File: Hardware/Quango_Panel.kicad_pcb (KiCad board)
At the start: 2 copper layers, 80.9 x 128.5 mm, 25 parts

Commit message: More schematic updates
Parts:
- added Ref**: Subminiature_Switch, Custom_Footprints:LED_Hole_3mm, F.Cu at (106.1, 42.6)
- added Ref**: Subminiature_Switch, Custom_Footprints:LED_Hole_3mm, F.Cu at (77.8, 42.6)
- added Ref**: Subminiature_Switch, Custom_Footprints:LED_Hole_3mm, F.Cu at (86.2, 42.6)
- added Ref**: Subminiature_Switch, Custom_Footprints:LED_Hole_3mm, F.Cu at (97.7, 42.6)
- moved REF** 21.2 mm to (100.3, 139.2)
- moved USB** 17.6 mm to (81.5, 141.1)
- moved Ref** 10.7 mm to (81.7, 127.7)
- moved REF** 9.72 mm to (80.0, 118.4)
- moved REF** 9.72 mm to (96.2, 118.6)
- moved Ref** 8.41 mm to (73.6, 42.6), turned to 90 degrees
- moved RESET 7.21 mm to (79.8, 48.6)
- moved RESET 6.28 mm to (100.0, 48.6)
- moved Ref** 5.61 mm to (101.9, 42.6), turned to 90 degrees
- moved Ref** 4.78 mm to (82.0, 42.6), turned to 90 degrees
- moved Ref** 2.01 mm to (93.5, 42.6), turned to 90 degrees

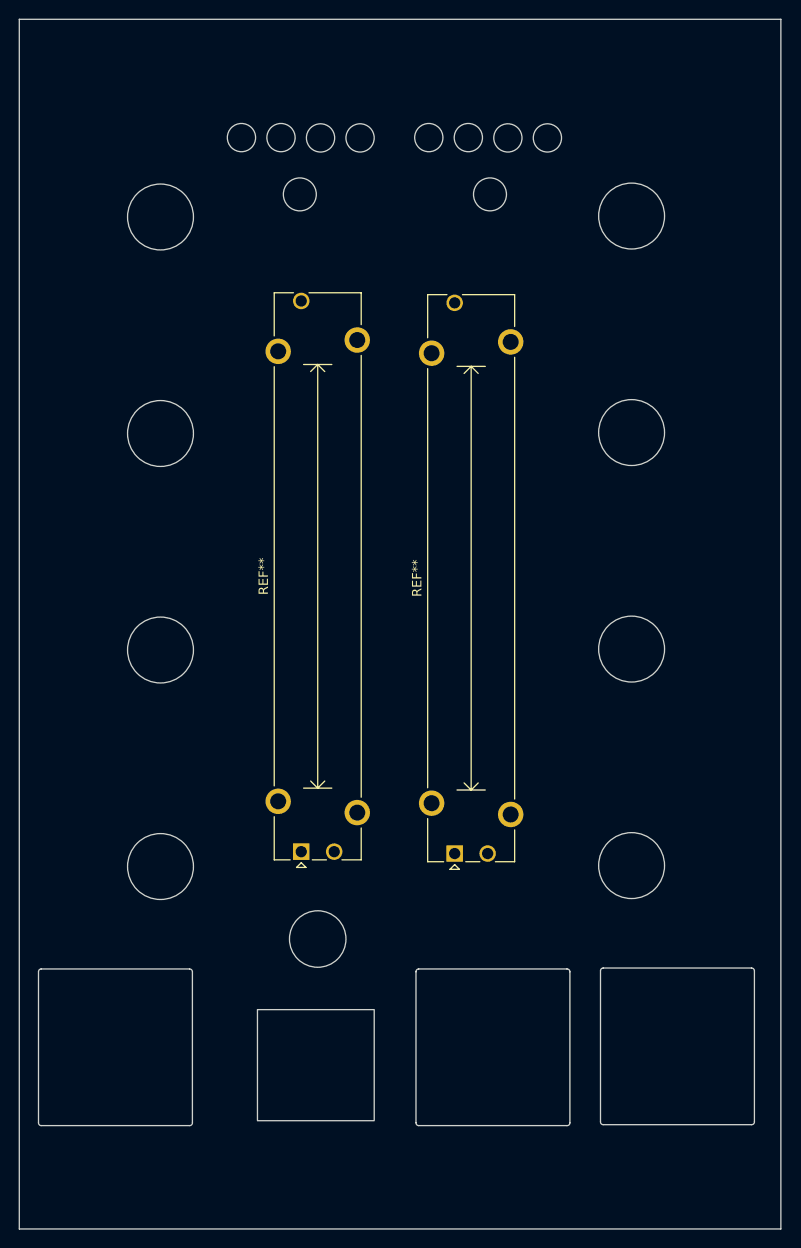
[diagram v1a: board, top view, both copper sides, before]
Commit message: Reduced module size to 14HP; updated to Amphenol USB C
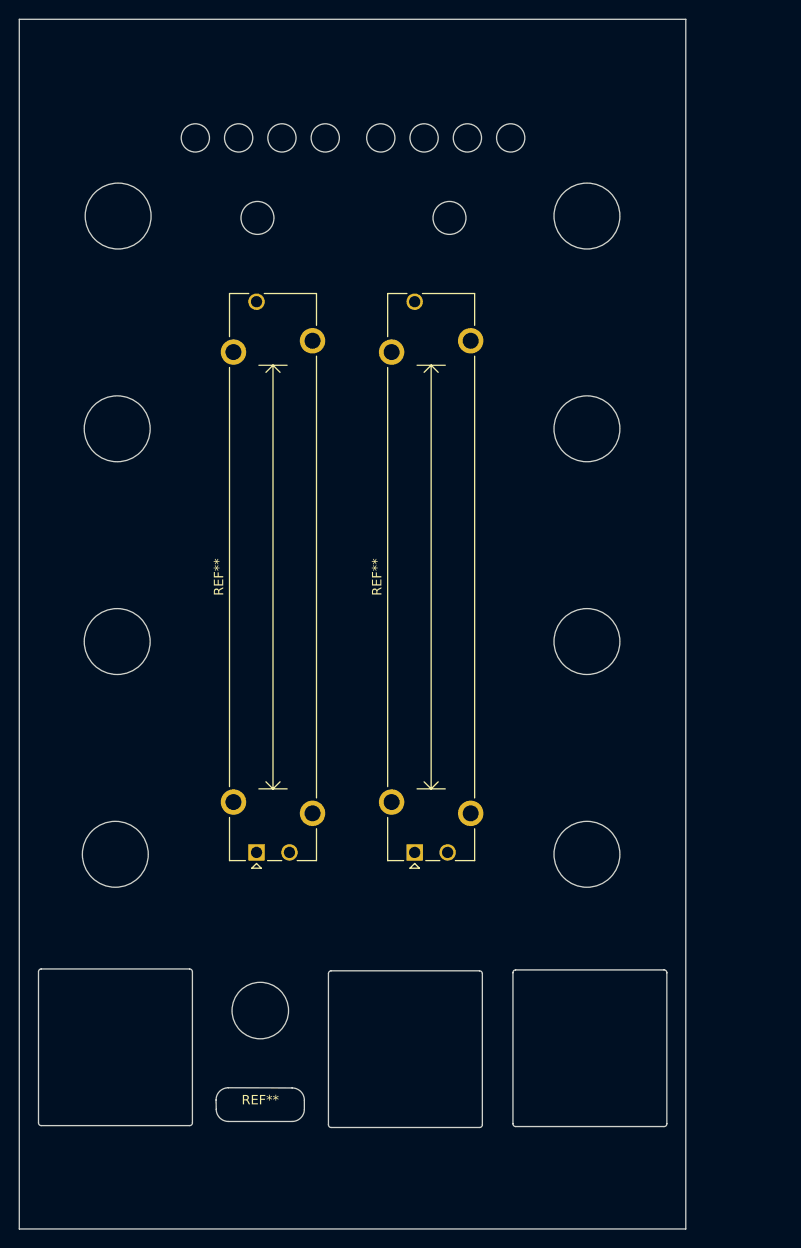
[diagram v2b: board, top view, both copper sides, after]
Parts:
- removed USB**: USB_B_CUTOUT, Custom_Footprints:USB_B_CUTOUT
- added REF**: USB_C_Cutout, Custom_Footprints:USB_C_Cutout, F.Cu at (75.6, 145.3)
- moved Ref** 9.75 mm to (75.6, 135.3)
- moved REF** 9.30 mm to (110.6, 139.3)
- moved REF** 9.30 mm to (91.0, 139.4)
- moved RESET 5.15 mm to (75.3, 51.1)
- moved Ref** 5.10 mm to (88.4, 42.6)
- moved RESET 4.97 mm to (95.7, 51.1)
- moved Ref** 4.97 mm to (60.2, 118.7)
- moved Ref** 4.90 mm to (68.7, 42.6)
- moved Ref** 4.89 mm to (110.3, 118.7)
- moved Ref** 4.81 mm to (110.3, 96.1)
- moved Ref** 4.76 mm to (110.3, 73.5)
- moved REF** 4.75 mm to (75.2, 118.5)
- moved Ref** 4.74 mm to (110.3, 50.9)
- moved Ref** 4.70 mm to (93.0, 42.6)
- moved Ref** 4.69 mm to (60.4, 96.1)
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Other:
- board size 80.9 x 128.5 mm -> 70.8 x 128.5 mm
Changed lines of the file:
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@@
   (net 0 "")
   (footprint "Custom_Footprints:LED_Hole_3mm" (layer "F.Cu")
-    (at 82 42.6 90)
+    (at 77.9 42.6 90)
     (descr "Mounting Hole 6mm, no annular")
     (tags "mounting hole 6mm no annular")
@@
   )
   (footprint "Potentiometer_THT:Potentiometer_Bourns_PTA4543_Single_Slide" (layer "F.Cu")
-    (at 79.95 118.42 90)
+    (at 75.2 118.5 90)
     (descr "Bourns single-gang slide potentiometer, 45.0mm travel, https://www.bourns.com/docs/Product-Datasheets/pta.pdf")
     (tags "Bourns single-gang slide potentiometer 45.0mm")
@@
   )
   (footprint "Custom_Footprints:RJ45_Molex_42878-8506_Mounting_Hole" (layer "F.Cu")
-    (at 100.3 139.2)
+    (at 91 139.4)
     (descr "RJ45 vertical connector https://www.on-shore.com/wp-content/uploads/PJ012-8P8CX.pdf")
     (tags "RJ45 PJ012")
@@
   )
   (footprint "Custom_Footprints:LED_Hole_3mm" (layer "F.Cu")
-    (at 93.5 42.566668 90)
+    (at 88.4 42.6 90)
     (descr "Mounting Hole 6mm, no annular")
     (tags "mounting hole 6mm no annular")
@@
   )
   (footprint "Custom_Footprints:LED_Hole_3mm" (layer "F.Cu")
-    (at 97.7 42.566668 90)
+    (at 93 42.6 90)
     (descr "Mounting Hole 6mm, no annular")
     (tags "mounting hole 6mm no annular")
@@
   )
   (footprint "Custom_Footprints:Alpha_9mm_pot_hole" (layer "F.Cu")
-    (at 65 51)
+    (at 60.5 50.9)
     (descr "Mounting Hole 7mm")
     (tags "mounting hole 7mm")
@@
   )
   (footprint "Custom_Footprints:Alpha_9mm_pot_hole" (layer "F.Cu")
-    (at 115.042857 96.9)
+    (at 110.3 96.1)
     (descr "Mounting Hole 7mm")
     (tags "mounting hole 7mm")
@@
   )
   (footprint "Custom_Footprints:Thonkiconn_Socket_MountingHole_6mm" (layer "F.Cu")
-    (at 81.7 127.7)
+    (at 75.6 135.3)
     (descr "Mounting Hole 6mm, no annular")
     (tags "mounting hole 6mm no annular")
@@
   )
   (footprint "Potentiometer_THT:Potentiometer_Bourns_PTA4543_Single_Slide" (layer "F.Cu")
-    (at 96.25 118.62 90)
+    (at 92 118.5 90)
     (descr "Bourns single-gang slide potentiometer, 45.0mm travel, https://www.bourns.com/docs/Product-Datasheets/pta.pdf")
     (tags "Bourns single-gang slide potentiometer 45.0mm")
@@
   )
   (footprint "Custom_Footprints:Alpha_9mm_pot_hole" (layer "F.Cu")
-    (at 65 120)
+    (at 60.2 118.7)
     (descr "Mounting Hole 7mm")
     (tags "mounting hole 7mm")
@@
   )
   (footprint "Custom_Footprints:Alpha_9mm_pot_hole" (layer "F.Cu")
-    (at 115.042857 73.9)
+    (at 110.3 73.5)
     (descr "Mounting Hole 7mm")
     (tags "mounting hole 7mm")
@@
     )
   )
-  (footprint "Custom_Footprints:USB_B_CUTOUT" (layer "F.Cu")
-    (at 81.5 141.1)
-    (attr smd)
-    (fp_text reference "USB**" (at 0 -7 unlocked) (layer "F.SilkS") hide
-      (effects (font (size 1 1) (thickness 0.15)))
-    )
-    (fp_text value "USB_B_CUTOUT" (at 0.5 8.3 unlocked) (layer "F.Fab")
-      (effects (font (size 1 1) (thickness 0.15)))
-    )
-    (fp_text user "${REFERENCE}" (at 0.2 10.3 unlocked) (layer "F.Fab")
-      (effects (font (size 1 1) (thickness 0.15)))
-    )
-    (fp_rect (start -6.2 -5.9) (end 6.2 5.9) (layer "Edge.Cuts") (width 0.1) (fill none))
-    (fp_rect (start -9.75 -7.4) (end 9.75 7.4) (layer "F.CrtYd") (width 0.05) (fill none))
-    (model "${CUSTOM_3D}/USB_TE_1734517-1.step"
-      (offset (xyz 0 0 0.5))
-      (scale (xyz 1 1 1))
-      (rotate (xyz 0 0 0))
-    )
-  )
   (footprint "Custom_Footprints:LED_Hole_3mm" (layer "F.Cu")
-    (at 73.6 42.566666 90)
+    (at 68.7 42.6 90)
     (descr "Mounting Hole 6mm, no annular")
     (tags "mounting hole 6mm no annular")
@@
   )
   (footprint "Custom_Footprints:LED_Hole_3mm" (layer "F.Cu")
-    (at 101.9 42.6 90)
+    (at 97.6 42.6 90)
     (descr "Mounting Hole 6mm, no annular")
     (tags "mounting hole 6mm no annular")
@@
   )
   (footprint "Custom_Footprints:Alpha_9mm_pot_hole" (layer "F.Cu")
-    (at 115.042857 50.9)
+    (at 110.3 50.9)
     (descr "Mounting Hole 7mm")
     (tags "mounting hole 7mm")
@@
   )
   (footprint "Custom_Footprints:Alpha_9mm_pot_hole" (layer "F.Cu")
-    (at 115.042857 119.9)
+    (at 110.3 118.7)
     (descr "Mounting Hole 7mm")
     (tags "mounting hole 7mm")
@@
   )
   (footprint "Custom_Footprints:Alpha_9mm_pot_hole" (layer "F.Cu")
-    (at 65 97)
+    (at 60.4 96.1)
     (descr "Mounting Hole 7mm")
     (tags "mounting hole 7mm")
@@
     )
   )
+  (footprint "Custom_Footprints:USB_C_Cutout" (layer "F.Cu")
+    (at 75.6 145.3)
+    (attr smd)
+    (fp_text reference "REF**" (at 0 -0.5 unlocked) (layer "F.SilkS")
+      (effects (font (size 1 1) (thickness 0.15)))
+    )
+    (fp_text value "USB_C_Cutout" (at 0 1 unlocked) (layer "F.Fab")
+      (effects (font (size 1 1) (thickness 0.15)))
+    )
+    (fp_text user "${REFERENCE}" (at 0 2.5 unlocked) (layer "F.Fab")
+      (effects (font (size 1 1) (thickness 0.15)))
+    )
+    (fp_rect (start -4.6 -1.7) (end 4.6 1.7) (layer "Dwgs.User") (width 0.12) (fill none))
+    (fp_line (start -4.7 -0.5) (end -4.680761 0.480761) (layer "Edge.Cuts") (width 0.12))
+    (fp_line (start 4.680761 0.480761) (end 4.680761 -0.480761) (layer "Edge.Cuts") (width 0.12))
+    (fp_line (start -3.4 -1.8) (end 3.380761 -1.780761) (layer "Edge.Cuts") (width 0.12))
+    (fp_line (start -3.380761 1.780761) (end 3.380761 1.780761) (layer "Edge.Cuts") (width 0.12))
+    (fp_arc (start -4.7 -0.5) (mid -4.319239 -1.419239) (end -3.4 -1.8) (layer "Edge.Cuts") (width 0.12))
+    (fp_arc (start -3.380761 1.780761) (mid -4.3 1.4) (end -4.680761 0.480761) (layer "Edge.Cuts") (width 0.12))
+    (fp_arc (start 4.680761 0.480761) (mid 4.3 1.4) (end 3.380761 1.780761) (layer "Edge.Cuts") (width 0.12))
+    (fp_arc (start 3.380761 -1.780761) (mid 4.3 -1.4) (end 4.680761 -0.480761) (layer "Edge.Cuts") (width 0.12))
+    (model "${CUSTOM_3D}/DX07S024WJ3R400--3DModel-STEP-56544.STEP" hide
+      (offset (xyz 0 0 -10))
+      (scale (xyz 1 1 1))
+      (rotate (xyz -90 0 0))
+    )
+    (model "${CUSTOM_3D}/12401951E412A--3DModel-STEP-533217.STEP"
+      (offset (xyz -4.5 -1.2 -8))
+      (scale (xyz 1 1 1))
+      (rotate (xyz 0 90 0))
+    )
+  )
   (footprint "Custom_Footprints:RJ45_Molex_42878-8506_Mounting_Hole" (layer "F.Cu")
-    (at 119.9 139.1)
+    (at 110.6 139.3)
     (descr "RJ45 vertical connector https://www.on-shore.com/wp-content/uploads/PJ012-8P8CX.pdf")
     (tags "RJ45 PJ012")
@@
   )
   (footprint "Custom_Footprints:Alpha_9mm_pot_hole" (layer "F.Cu")
-    (at 65 74)
+    (at 60.4 73.5)
     (descr "Mounting Hole 7mm")
     (tags "mounting hole 7mm")
@@
   )
   (footprint "Custom_Footprints:LED_Hole_3mm" (layer "F.Cu")
-    (at 106.1 42.6 90)
+    (at 102.2 42.6 90)
     (descr "Mounting Hole 6mm, no annular")
     (tags "mounting hole 6mm no annular")
@@
   )
   (footprint "Custom_Footprints:LED_Hole_3mm" (layer "F.Cu")
-    (at 77.8 42.566666 90)
+    (at 73.3 42.6 90)
     (descr "Mounting Hole 6mm, no annular")
     (tags "mounting hole 6mm no annular")
@@
   )
   (footprint "Custom_Footprints:LED_Hole_3mm" (layer "F.Cu")
-    (at 86.2 42.6 90)
+    (at 82.5 42.6 90)
     (descr "Mounting Hole 6mm, no annular")
     (tags "mounting hole 6mm no annular")
@@
   )
   (footprint "Custom_Footprints:Small_Pushbutton_Hole_3.5mm" (layer "B.Cu")
-    (at 79.8 48.6)
+    (at 75.3 51.1)
     (descr "Button Hole 3.5mm")
     (attr through_hole)
@@
   )
   (footprint "Custom_Footprints:Small_Pushbutton_Hole_3.5mm" (layer "B.Cu")
-    (at 100 48.6)
+    (at 95.7 51.1)
     (descr "Button Hole 3.5mm")
     (attr through_hole)
@@
   )
   (gr_rect (start 50.1 39) (end 130.8 149) (layer "Dwgs.User") (width 0.15) (fill none))
-  (gr_rect (start 50 30) (end 130.9 158.5) (layer "Edge.Cuts") (width 0.1) (fill none))
+  (gr_line (start 85.4 29) (end 85.4 160.6) (layer "Dwgs.User") (width 0.15))
+  (gr_rect (start 50 30) (end 120.8 158.5) (layer "Edge.Cuts") (width 0.1) (fill none))
 )

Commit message: Added individual audio channel breakout
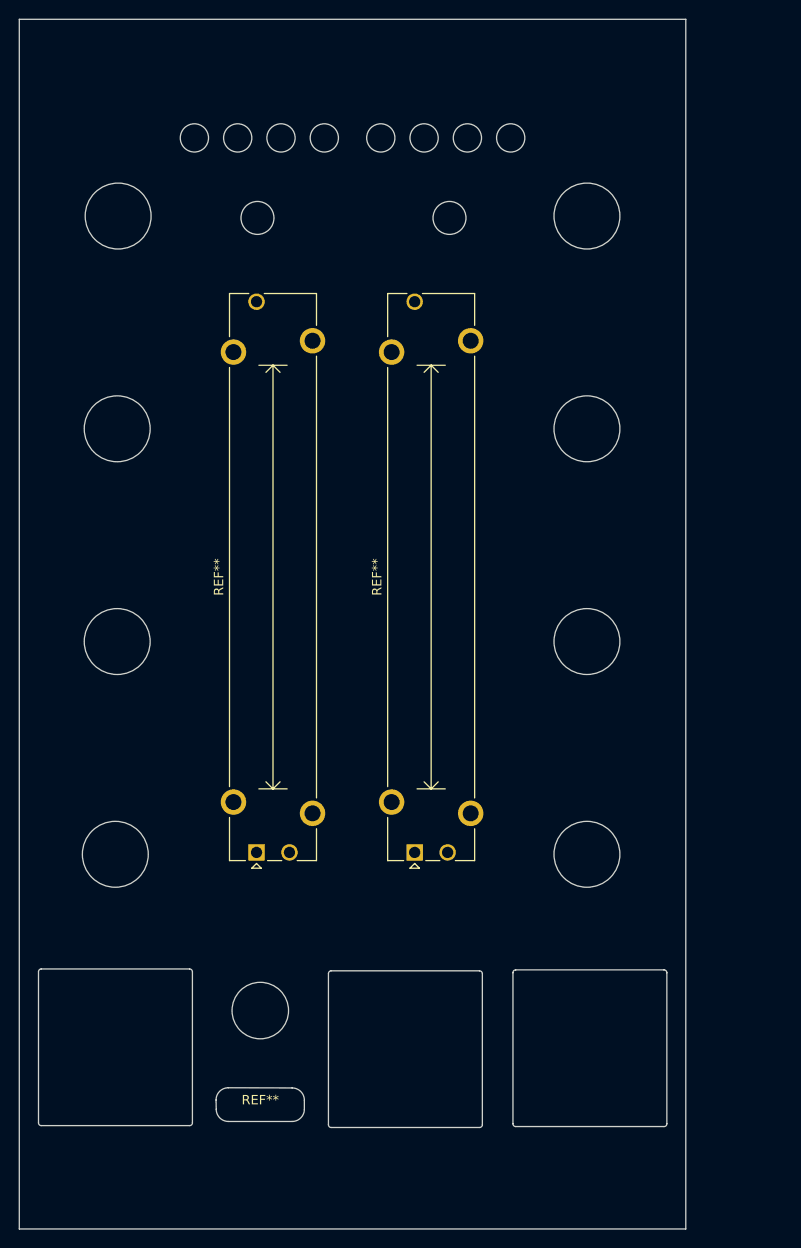
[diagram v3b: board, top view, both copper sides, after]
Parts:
- moved Ref** 0.10 mm to (77.8, 42.6)
- moved Ref** 0.10 mm to (68.6, 42.6)
- moved Ref** 0.10 mm to (73.2, 42.6)
- moved Ref** 0.10 mm to (82.4, 42.6)
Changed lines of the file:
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@@
   (net 0 "")
   (footprint "Custom_Footprints:LED_Hole_3mm" (layer "F.Cu")
-    (at 77.9 42.6 90)
+    (at 77.8 42.6 90)
     (descr "Mounting Hole 6mm, no annular")
     (tags "mounting hole 6mm no annular")
@@
     (fp_arc (start -7.88 8.32) (mid -8.081749 8.227632) (end -8.16 8.02) (layer "Edge.Cuts") (width 0.12))
     (fp_arc (start -8.16 -8.02) (mid -8.081443 -8.227347) (end -7.88 -8.32) (layer "Edge.Cuts") (width 0.12))
-    (fp_arc (start 7.88 -8.32) (mid 8.096622 -8.233665) (end 8.19 -8.02) (layer "Edge.Cuts") (width 0.12))
+    (fp_arc (start 7.88 -8.32) (mid 8.096588 -8.233658) (end 8.19 -8.02) (layer "Edge.Cuts") (width 0.12))
     (fp_arc (start 8.19 8.02) (mid 8.100917 8.238111) (end 7.88 8.32) (layer "Edge.Cuts") (width 0.12))
     (fp_line (start -8.31 -8.5) (end 8.39 -8.5) (layer "F.CrtYd") (width 0.05))
@@
     (fp_line (start 8.19 -8.02) (end 8.19 8.02) (layer "Edge.Cuts") (width 0.12))
     (fp_line (start 7.88 -8.32) (end -7.88 -8.32) (layer "Edge.Cuts") (width 0.12))
-    (fp_arc (start 7.88 -8.32) (mid 8.096622 -8.233665) (end 8.19 -8.02) (layer "Edge.Cuts") (width 0.12))
+    (fp_arc (start 7.88 -8.32) (mid 8.096588 -8.233658) (end 8.19 -8.02) (layer "Edge.Cuts") (width 0.12))
     (fp_arc (start -8.16 -8.02) (mid -8.081443 -8.227347) (end -7.88 -8.32) (layer "Edge.Cuts") (width 0.12))
     (fp_arc (start -7.88 8.32) (mid -8.081749 8.227632) (end -8.16 8.02) (layer "Edge.Cuts") (width 0.12))
@@
   )
   (footprint "Custom_Footprints:LED_Hole_3mm" (layer "F.Cu")
-    (at 68.7 42.6 90)
+    (at 68.6 42.6 90)
     (descr "Mounting Hole 6mm, no annular")
     (tags "mounting hole 6mm no annular")
@@
     (fp_arc (start 8.19 8.02) (mid 8.100917 8.238111) (end 7.88 8.32) (layer "Edge.Cuts") (width 0.12))
     (fp_arc (start -7.88 8.32) (mid -8.081749 8.227632) (end -8.16 8.02) (layer "Edge.Cuts") (width 0.12))
-    (fp_arc (start 7.88 -8.32) (mid 8.096622 -8.233665) (end 8.19 -8.02) (layer "Edge.Cuts") (width 0.12))
+    (fp_arc (start 7.88 -8.32) (mid 8.096588 -8.233658) (end 8.19 -8.02) (layer "Edge.Cuts") (width 0.12))
     (fp_line (start -8.31 -8.5) (end 8.39 -8.5) (layer "F.CrtYd") (width 0.05))
     (fp_line (start 8.39 -8.5) (end 8.39 8.5) (layer "F.CrtYd") (width 0.05))
@@
   )
   (footprint "Custom_Footprints:LED_Hole_3mm" (layer "F.Cu")
-    (at 73.3 42.6 90)
+    (at 73.2 42.6 90)
     (descr "Mounting Hole 6mm, no annular")
     (tags "mounting hole 6mm no annular")
@@
   )
   (footprint "Custom_Footprints:LED_Hole_3mm" (layer "F.Cu")
-    (at 82.5 42.6 90)
-    (descr "Mounting Hole 6mm, no annular")
-    (tags "mounting hole 6mm no annular")
+    (at 82.4 42.6 90)
+    (descr "Mounting Hole 6mm, no annular")
+    (tags "mounting hole 6mm no annular")
